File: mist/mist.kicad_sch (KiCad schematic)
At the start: 31 parts, among them J1 USB_C_Receptacle_USB2.0, J2 Conn_01x05, Q3 MMUN2133LT1G, U2 PRTR5V0U2X, U3 XC6206PxxxMR-Regulator_Linear, U4 CR2013-MI2120, U5 STM32G474RETx, U6 SN74AHCT1G125DBVR

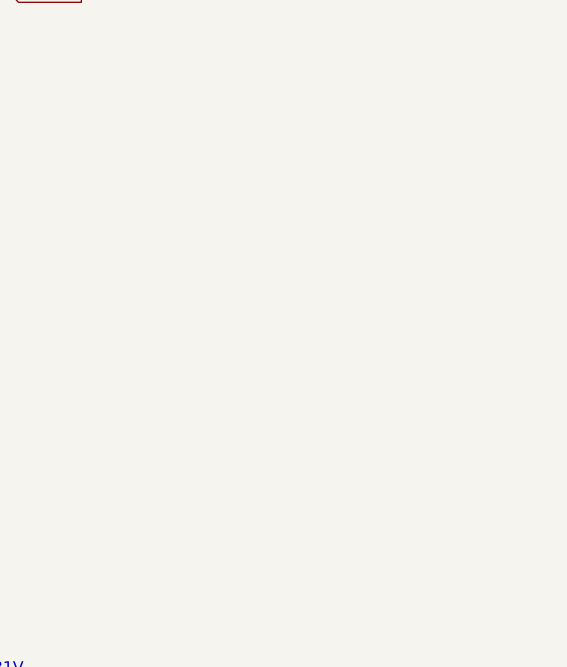
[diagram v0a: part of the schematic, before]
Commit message: Updated standoff sizes
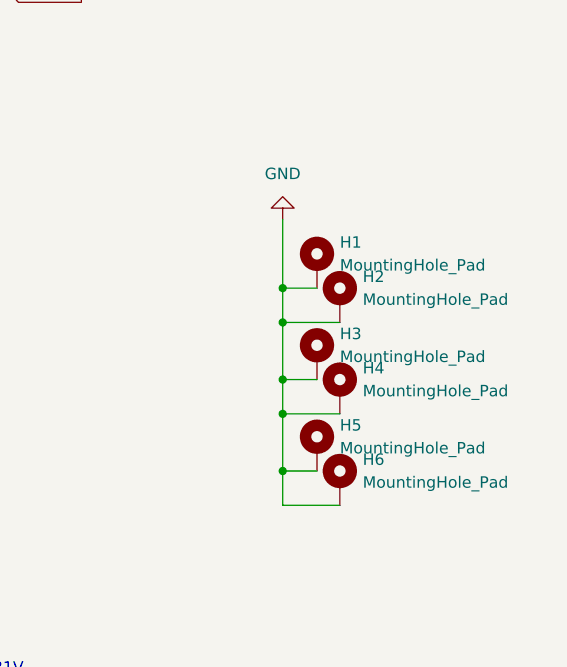
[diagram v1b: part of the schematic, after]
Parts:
- added H1, H2, H3, H4, H5, H6: MountingHole_Pad, MountingHole:MountingHole_3.2mm_M3_DIN965_Pad, symbol Mechanical:MountingHole_Pad
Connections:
- net GND: now also H1.1, H2.1, H3.1, H4.1, H5.1, H6.1
